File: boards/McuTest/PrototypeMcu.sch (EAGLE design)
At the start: 25 parts, among them IC1 REG1118, J1 10118193-0001LF, Q1 8MHz

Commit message: All wires traced but ground plane is not complete
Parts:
- removed JP2: (no value), pinhead:PINHD-1X6
- removed JP3: (no value), pinhead:PINHD-1X4
- added 5V___3.3V: (no value), pinhead:PINHD-1X4
- added JP4: (no value), pinhead:PINHD-1X3
- added JP5: (no value), pinhead:PINHD-2X8
- added S2, S3, SWD: (no value), pinhead:PINHD-1X2
- added SW1: B3U-1000P-2P-SMD, Seeed-Switch:SMD-BUTTON(2P-3.0X2.5X1.2+0.4MM)-B3U-1000P-2P-SMD
- D1: device diode:DIODE-DO201-15 -> diode:DIODE-SOD57-10
- R1: value 10Kohm -> 10K
- S1: device Wurth_Elektronik_Electromechanic_Switch_rev18c:4301X20738X6_430162073826 -> pinhead:PINHD-1X2
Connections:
- new net GPIO0: CR1.PB0, JP5.12
- new net GPIO1: CR1.PB1, JP5.14
- new net GPIO2: CR1.PB2, JP5.16
- new net GPIO4: CR1.PC4, JP5.8
- new net GPIO5: CR1.PC5, JP5.10
- new net N$10: CR1.PC6, JP5.7
- new net N$11: CR1.PB15, JP5.9
- new net N$12: CR1.PB14, JP5.11
- new net N$13: CR1.PB13, JP5.13
- new net N$14: CR1.PB12, JP5.15
- new net N$7: CR1.PC8, JP5.3
- new net N$9: CR1.PC7, JP5.5
- net GND: now also C5.2, JP4.1, JP4.2, JP4.3, JP5.2, JP5.4, JP5.6, SW1.1; no longer JP3.4, S1.2
- net N$3: now also CR1.PC9, JP5.1; no longer C5.2, S1.4
- net N$4: now also 5V___3.3V.3, 5V___3.3V.4
- net N$6: now also SWD.2; no longer JP3.2
- net N$8: now also SWD.1; no longer JP3.1
- net N_RST: now also SW1.2; no longer S1.3
- net USART1_RX: now also S1.1; no longer JP2.1
- net USART1_TX: now also S1.2; no longer JP2.2
- net USART2_RX: now also S2.1; no longer JP2.3
- net USART2_TX: now also S2.2; no longer JP2.4
- net USART3_RX: now also S3.1; no longer JP2.5
- net USART3_TX: now also S3.2; no longer JP2.6
- net VDD: now also 5V___3.3V.1, 5V___3.3V.2; no longer JP3.3, S1.1

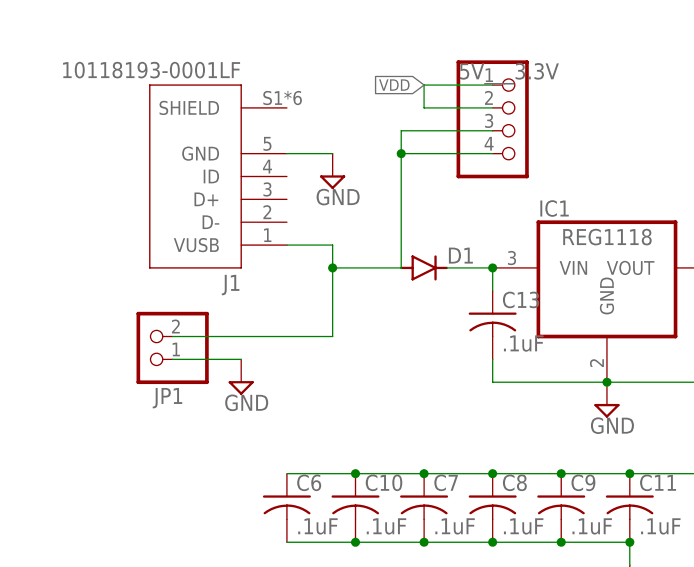
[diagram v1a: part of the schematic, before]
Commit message: Added a fuse and impedance matched clock signals
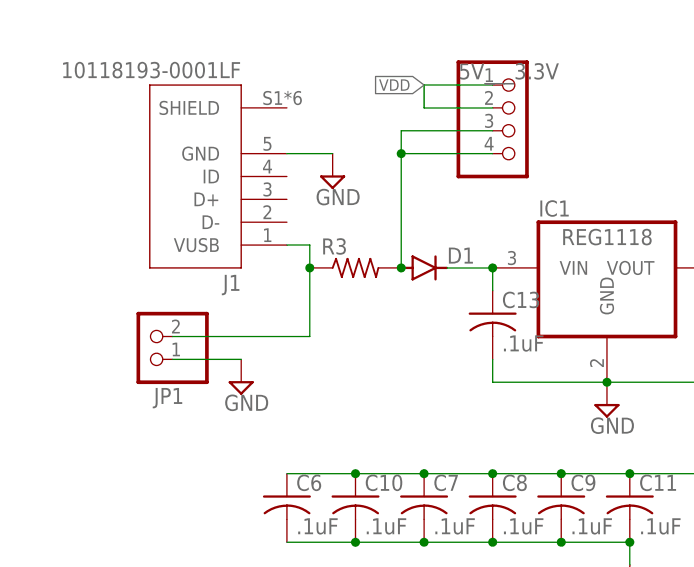
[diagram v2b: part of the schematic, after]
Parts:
- added R3: (no value), rcl:R-US_M1206
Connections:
- new net N$16: J1.VUSB, JP1.2, R3.1
- net N$4: now also R3.2; no longer J1.VUSB, JP1.2
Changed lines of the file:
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@@
 <grid distance="0.1" unitdist="inch" unit="inch" style="lines" multiple="1" display="no" altdistance="0.01" altunitdist="inch" altunit="inch"/>
 <layers>
-<layer number="1" name="Top" color="4" fill="1" visible="yes" active="no"/>
-<layer number="2" name="Route2" color="16" fill="1" visible="yes" active="no"/>
-<layer number="3" name="Route3" color="17" fill="1" visible="yes" active="no"/>
-<layer number="4" name="Route4" color="18" fill="1" visible="yes" active="no"/>
-<layer number="5" name="Route5" color="19" fill="1" visible="yes" active="no"/>
-<layer number="6" name="Route6" color="25" fill="1" visible="yes" active="no"/>
-<layer number="7" name="Route7" color="26" fill="1" visible="yes" active="no"/>
-<layer number="8" name="Route8" color="27" fill="1" visible="yes" active="no"/>
-<layer number="9" name="Route9" color="28" fill="1" visible="yes" active="no"/>
-<layer number="10" name="Route10" color="29" fill="1" visible="yes" active="no"/>
-<layer number="11" name="Route11" color="30" fill="1" visible="yes" active="no"/>
-<layer number="12" name="Route12" color="20" fill="1" visible="yes" active="no"/>
-<layer number="13" name="Route13" color="21" fill="1" visible="yes" active="no"/>
-<layer number="14" name="Route14" color="22" fill="1" visible="yes" active="no"/>
-<layer number="15" name="Route15" color="23" fill="1" visible="yes" active="no"/>
-<layer number="16" name="Bottom" color="1" fill="1" visible="yes" active="no"/>
-<layer number="17" name="Pads" color="2" fill="1" visible="yes" active="no"/>
-<layer number="18" name="Vias" color="2" fill="1" visible="yes" active="no"/>
-<layer number="19" name="Unrouted" color="6" fill="1" visible="yes" active="no"/>
-<layer number="20" name="Dimension" color="24" fill="1" visible="yes" active="no"/>
-<layer number="21" name="tPlace" color="7" fill="1" visible="yes" active="no"/>
-<layer number="22" name="bPlace" color="7" fill="1" visible="yes" active="no"/>
-<layer number="23" name="tOrigins" color="15" fill="1" visible="yes" active="no"/>
-<layer number="24" name="bOrigins" color="15" fill="1" visible="yes" active="no"/>
-<layer number="25" name="tNames" color="7" fill="1" visible="yes" active="no"/>
-<layer number="26" name="bNames" color="7" fill="1" visible="yes" active="no"/>
-<layer number="27" name="tValues" color="7" fill="1" visible="yes" active="no"/>
-<layer number="28" name="bValues" color="7" fill="1" visible="yes" active="no"/>
+<layer number="1" name="Top" color="4" fill="1" visible="no" active="no"/>
+<layer number="2" name="Route2" color="16" fill="1" visible="no" active="no"/>
+<layer number="3" name="Route3" color="17" fill="1" visible="no" active="no"/>
+<layer number="4" name="Route4" color="18" fill="1" visible="no" active="no"/>
+<layer number="5" name="Route5" color="19" fill="1" visible="no" active="no"/>
+<layer number="6" name="Route6" color="25" fill="1" visible="no" active="no"/>
+<layer number="7" name="Route7" color="26" fill="1" visible="no" active="no"/>
+<layer number="8" name="Route8" color="27" fill="1" visible="no" active="no"/>
+<layer number="9" name="Route9" color="28" fill="1" visible="no" active="no"/>
+<layer number="10" name="Route10" color="29" fill="1" visible="no" active="no"/>
+<layer number="11" name="Route11" color="30" fill="1" visible="no" active="no"/>
+<layer number="12" name="Route12" color="20" fill="1" visible="no" active="no"/>
+<layer number="13" name="Route13" color="21" fill="1" visible="no" active="no"/>
+<layer number="14" name="Route14" color="22" fill="1" visible="no" active="no"/>
+<layer number="15" name="Route15" color="23" fill="1" visible="no" active="no"/>
+<layer number="16" name="Bottom" color="1" fill="1" visible="no" active="no"/>
+<layer number="17" name="Pads" color="2" fill="1" visible="no" active="no"/>
+<layer number="18" name="Vias" color="2" fill="1" visible="no" active="no"/>
+<layer number="19" name="Unrouted" color="6" fill="1" visible="no" active="no"/>
+<layer number="20" name="Dimension" color="24" fill="1" visible="no" active="no"/>
+<layer number="21" name="tPlace" color="7" fill="1" visible="no" active="no"/>
+<layer number="22" name="bPlace" color="7" fill="1" visible="no" active="no"/>
+<layer number="23" name="tOrigins" color="15" fill="1" visible="no" active="no"/>
+<layer number="24" name="bOrigins" color="15" fill="1" visible="no" active="no"/>
+<layer number="25" name="tNames" color="7" fill="1" visible="no" active="no"/>
+<layer number="26" name="bNames" color="7" fill="1" visible="no" active="no"/>
+<layer number="27" name="tValues" color="7" fill="1" visible="no" active="no"/>
+<layer number="28" name="bValues" color="7" fill="1" visible="no" active="no"/>
 <layer number="29" name="tStop" color="7" fill="3" visible="no" active="no"/>
 <layer number="30" name="bStop" color="7" fill="6" visible="no" active="no"/>
@@
 <layer number="35" name="tGlue" color="7" fill="4" visible="no" active="no"/>
 <layer number="36" name="bGlue" color="7" fill="5" visible="no" active="no"/>
-<layer number="37" name="tTest" color="7" fill="1" visible="yes" active="no"/>
-<layer number="38" name="bTest" color="7" fill="1" visible="yes" active="no"/>
+<layer number="37" name="tTest" color="7" fill="1" visible="no" active="no"/>
+<layer number="38" name="bTest" color="7" fill="1" visible="no" active="no"/>
 <layer number="39" name="tKeepout" color="4" fill="11" visible="no" active="no"/>
 <layer number="40" name="bKeepout" color="1" fill="11" visible="no" active="no"/>
@@
 <layer number="44" name="Drills" color="7" fill="1" visible="no" active="no"/>
 <layer number="45" name="Holes" color="7" fill="1" visible="no" active="no"/>
-<layer number="46" name="Milling" color="3" fill="1" visible="yes" active="no"/>
-<layer number="47" name="Measures" color="7" fill="1" visible="yes" active="no"/>
-<layer number="48" name="Document" color="7" fill="1" visible="yes" active="no"/>
-<layer number="49" name="Reference" color="7" fill="1" visible="yes" active="no"/>
-<layer number="50" name="dxf" color="7" fill="1" visible="yes" active="no"/>
-<layer number="51" name="tDocu" color="7" fill="1" visible="yes" active="no"/>
-<layer number="52" name="bDocu" color="7" fill="1" visible="yes" active="no"/>
+<layer number="46" name="Milling" color="3" fill="1" visible="no" active="no"/>
+<layer number="47" name="Measures" color="7" fill="1" visible="no" active="no"/>
+<layer number="48" name="Document" color="7" fill="1" visible="no" active="no"/>
+<layer number="49" name="Reference" color="7" fill="1" visible="no" active="no"/>
+<layer number="50" name="dxf" color="7" fill="1" visible="no" active="no"/>
+<layer number="51" name="tDocu" color="7" fill="1" visible="no" active="no"/>
+<layer number="52" name="bDocu" color="7" fill="1" visible="no" active="no"/>
 <layer number="53" name="tGND_GNDA" color="7" fill="9" visible="no" active="no"/>
 <layer number="54" name="bGND_GNDA" color="1" fill="9" visible="no" active="no"/>
@@
 <part name="S1" library="pinhead" library_urn="urn:adsk.eagle:library:325" deviceset="PINHD-1X2" device="" package3d_urn="urn:adsk.eagle:package:22435/2"/>
 <part name="SUPPLY10" library="supply2" library_urn="urn:adsk.eagle:library:372" deviceset="GND" device=""/>
+<part name="R3" library="rcl" library_urn="urn:adsk.eagle:library:334" deviceset="R-US_" device="M1206" package3d_urn="urn:adsk.eagle:package:23566/1"/>
 </parts>
 <sheets>
@@
 <instance part="SUPPLY10" gate="GND" x="238.76" y="68.58" smashed="yes">
 <attribute name="VALUE" x="236.855" y="65.405" size="1.778" layer="96"/>
+</instance>
+<instance part="R3" gate="G$1" x="33.02" y="50.8" smashed="yes">
+<attribute name="NAME" x="29.21" y="52.2986" size="1.778" layer="95"/>
+<attribute name="VALUE" x="29.21" y="47.498" size="1.778" layer="96"/>
 </instance>
 </instances>
@@
 <net name="N$4" class="0">
 <segment>
-<pinref part="JP1" gate="G$1" pin="2"/>
-<wire x1="12.7" y1="43.18" x2="30.48" y2="43.18" width="0.1524" layer="91"/>
-<wire x1="30.48" y1="43.18" x2="30.48" y2="50.8" width="0.1524" layer="91"/>
-<pinref part="J1" gate="G$1" pin="VUSB"/>
-<wire x1="30.48" y1="50.8" x2="30.48" y2="53.34" width="0.1524" layer="91"/>
-<wire x1="25.4" y1="53.34" x2="30.48" y2="53.34" width="0.1524" layer="91"/>
 <pinref part="D1" gate="G$1" pin="A"/>
-<wire x1="30.48" y1="50.8" x2="38.1" y2="50.8" width="0.1524" layer="91"/>
-<junction x="30.48" y="50.8"/>
 <wire x1="38.1" y1="50.8" x2="38.1" y2="63.5" width="0.1524" layer="91"/>
 <pinref part="5V___3.3V" gate="A" pin="4"/>
@@
 <pinref part="5V___3.3V" gate="A" pin="3"/>
 <wire x1="38.1" y1="66.04" x2="48.26" y2="66.04" width="0.1524" layer="91"/>
+<pinref part="R3" gate="G$1" pin="2"/>
+<junction x="38.1" y="50.8"/>
 </segment>
 </net>
@@
 </segment>
 </net>
+<net name="N$16" class="0">
+<segment>
+<pinref part="JP1" gate="G$1" pin="2"/>
+<wire x1="12.7" y1="43.18" x2="27.94" y2="43.18" width="0.1524" layer="91"/>
+<pinref part="R3" gate="G$1" pin="1"/>
+<wire x1="27.94" y1="43.18" x2="27.94" y2="50.8" width="0.1524" layer="91"/>
+<pinref part="J1" gate="G$1" pin="VUSB"/>
+<wire x1="25.4" y1="53.34" x2="27.94" y2="53.34" width="0.1524" layer="91"/>
+<wire x1="27.94" y1="53.34" x2="27.94" y2="50.8" width="0.1524" layer="91"/>
+<junction x="27.94" y="50.8"/>
+</segment>
+</net>

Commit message: LED and silkscreen Aded
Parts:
- added LED1: (no value), led:LEDCHIPLED_0603
- added R4: 200, rcl:R-US_R0402
- SWD: device pinhead:PINHD-1X2 -> pinhead:PINHD-1X3
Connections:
- new net N$15: LED1.C, R4.1
- net GND: now also R4.2, SWD.3
- net VDD: now also LED1.A
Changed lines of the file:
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@@
 <part name="SUPPLY7" library="supply2" library_urn="urn:adsk.eagle:library:372" deviceset="GND" device=""/>
 <part name="SUPPLY8" library="supply2" library_urn="urn:adsk.eagle:library:372" deviceset="GND" device=""/>
-<part name="SWD" library="pinhead" library_urn="urn:adsk.eagle:library:325" deviceset="PINHD-1X2" device="" package3d_urn="urn:adsk.eagle:package:22435/2"/>
+<part name="SWD" library="pinhead" library_urn="urn:adsk.eagle:library:325" deviceset="PINHD-1X3" device="" package3d_urn="urn:adsk.eagle:package:22458/2"/>
 <part name="R2" library="rcl" library_urn="urn:adsk.eagle:library:334" deviceset="R-US_" device="R0402" package3d_urn="urn:adsk.eagle:package:23547/3" value="200"/>
 <part name="SW1" library="Seeed-Switch" library_urn="urn:adsk.eagle:library:476" deviceset="SMD-BUTTON(2P-3.0X2.5X1.2+0.4MM)" device="-B3U-1000P-2P-SMD" package3d_urn="urn:adsk.eagle:package:32999/1" value="B3U-1000P-2P-SMD"/>
@@
 <part name="SUPPLY10" library="supply2" library_urn="urn:adsk.eagle:library:372" deviceset="GND" device=""/>
 <part name="R3" library="rcl" library_urn="urn:adsk.eagle:library:334" deviceset="R-US_" device="M1206" package3d_urn="urn:adsk.eagle:package:23566/1"/>
+<part name="LED1" library="led" library_urn="urn:adsk.eagle:library:259" deviceset="LED" device="CHIPLED_0603" package3d_urn="urn:adsk.eagle:package:15822/2"/>
+<part name="R4" library="rcl" library_urn="urn:adsk.eagle:library:334" deviceset="R-US_" device="R0402" package3d_urn="urn:adsk.eagle:package:23547/3" value="200"/>
+<part name="SUPPLY11" library="supply2" library_urn="urn:adsk.eagle:library:372" deviceset="GND" device=""/>
+<part name="SUPPLY12" library="supply2" library_urn="urn:adsk.eagle:library:372" deviceset="GND" device=""/>
 </parts>
 <sheets>
@@
 </instance>
 <instance part="R1" gate="G$1" x="200.66" y="134.62" smashed="yes">
-<attribute name="NAME" x="196.85" y="136.1186" size="1.778" layer="95"/>
+<attribute name="NAME" x="199.39" y="136.1186" size="1.778" layer="95"/>
 <attribute name="VALUE" x="196.85" y="131.318" size="1.778" layer="96"/>
 </instance>
@@
 <attribute name="VALUE" x="28.575" y="57.785" size="1.778" layer="96"/>
 </instance>
-<instance part="SWD" gate="G$1" x="213.36" y="106.68" smashed="yes">
+<instance part="SWD" gate="A" x="213.36" y="106.68" smashed="yes">
 <attribute name="NAME" x="207.01" y="114.935" size="1.778" layer="95"/>
 <attribute name="VALUE" x="207.01" y="99.06" size="1.778" layer="96"/>
@@
 <attribute name="NAME" x="29.21" y="52.2986" size="1.778" layer="95"/>
 <attribute name="VALUE" x="29.21" y="47.498" size="1.778" layer="96"/>
+</instance>
+<instance part="LED1" gate="G$1" x="66.04" y="81.28" smashed="yes">
+<attribute name="NAME" x="69.596" y="76.708" size="1.778" layer="95" rot="R90"/>
+<attribute name="VALUE" x="71.755" y="76.708" size="1.778" layer="96" rot="R90"/>
+</instance>
+<instance part="R4" gate="G$1" x="66.04" y="71.12" smashed="yes" rot="MR270">
+<attribute name="NAME" x="64.5414" y="72.39" size="1.778" layer="95" rot="MR270"/>
+<attribute name="VALUE" x="69.342" y="74.93" size="1.778" layer="96" rot="MR270"/>
+</instance>
+<instance part="SUPPLY11" gate="GND" x="66.04" y="63.5" smashed="yes">
+<attribute name="VALUE" x="64.135" y="60.325" size="1.778" layer="96"/>
+</instance>
+<instance part="SUPPLY12" gate="GND" x="205.74" y="101.6" smashed="yes">
+<attribute name="VALUE" x="203.835" y="98.425" size="1.778" layer="96"/>
 </instance>
 </instances>
@@
 <junction x="238.76" y="73.66"/>
 </segment>
+<segment>
+<pinref part="R4" gate="G$1" pin="2"/>
+<pinref part="SUPPLY11" gate="GND" pin="GND"/>
+</segment>
+<segment>
+<pinref part="SWD" gate="A" pin="3"/>
+<pinref part="SUPPLY12" gate="GND" pin="GND"/>
+<wire x1="210.82" y1="104.14" x2="205.74" y2="104.14" width="0.1524" layer="91"/>
+</segment>
 </net>
 <net name="OSC8_IN" class="0">
@@
 <wire x1="40.64" y1="71.12" x2="40.64" y2="68.58" width="0.1524" layer="91"/>
 </segment>
+<segment>
+<pinref part="LED1" gate="G$1" pin="A"/>
+<wire x1="66.04" y1="83.82" x2="66.04" y2="88.9" width="0.1524" layer="91"/>
+<wire x1="66.04" y1="88.9" x2="58.42" y2="88.9" width="0.1524" layer="91"/>
+<label x="58.42" y="88.9" size="1.27" layer="95" rot="R180" xref="yes"/>
+</segment>
 </net>
 <net name="N$2" class="0">
@@
 <wire x1="182.88" y1="99.06" x2="203.2" y2="99.06" width="0.1524" layer="91"/>
 <wire x1="203.2" y1="99.06" x2="203.2" y2="106.68" width="0.1524" layer="91"/>
-<pinref part="SWD" gate="G$1" pin="2"/>
+<pinref part="SWD" gate="A" pin="2"/>
 <wire x1="203.2" y1="106.68" x2="210.82" y2="106.68" width="0.1524" layer="91"/>
 </segment>
@@
 <wire x1="182.88" y1="106.68" x2="200.66" y2="106.68" width="0.1524" layer="91"/>
 <wire x1="200.66" y1="106.68" x2="200.66" y2="109.22" width="0.1524" layer="91"/>
-<pinref part="SWD" gate="G$1" pin="1"/>
+<pinref part="SWD" gate="A" pin="1"/>
 <wire x1="200.66" y1="109.22" x2="210.82" y2="109.22" width="0.1524" layer="91"/>
 </segment>
@@
 </segment>
 </net>
+<net name="N$15" class="0">
+<segment>
+<pinref part="LED1" gate="G$1" pin="C"/>
+<pinref part="R4" gate="G$1" pin="1"/>
+</segment>
+</net>
